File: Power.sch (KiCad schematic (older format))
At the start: 21 parts, among them Q1 DMG3405, U6 MCP73831-2-OT, U7 TPS737xx

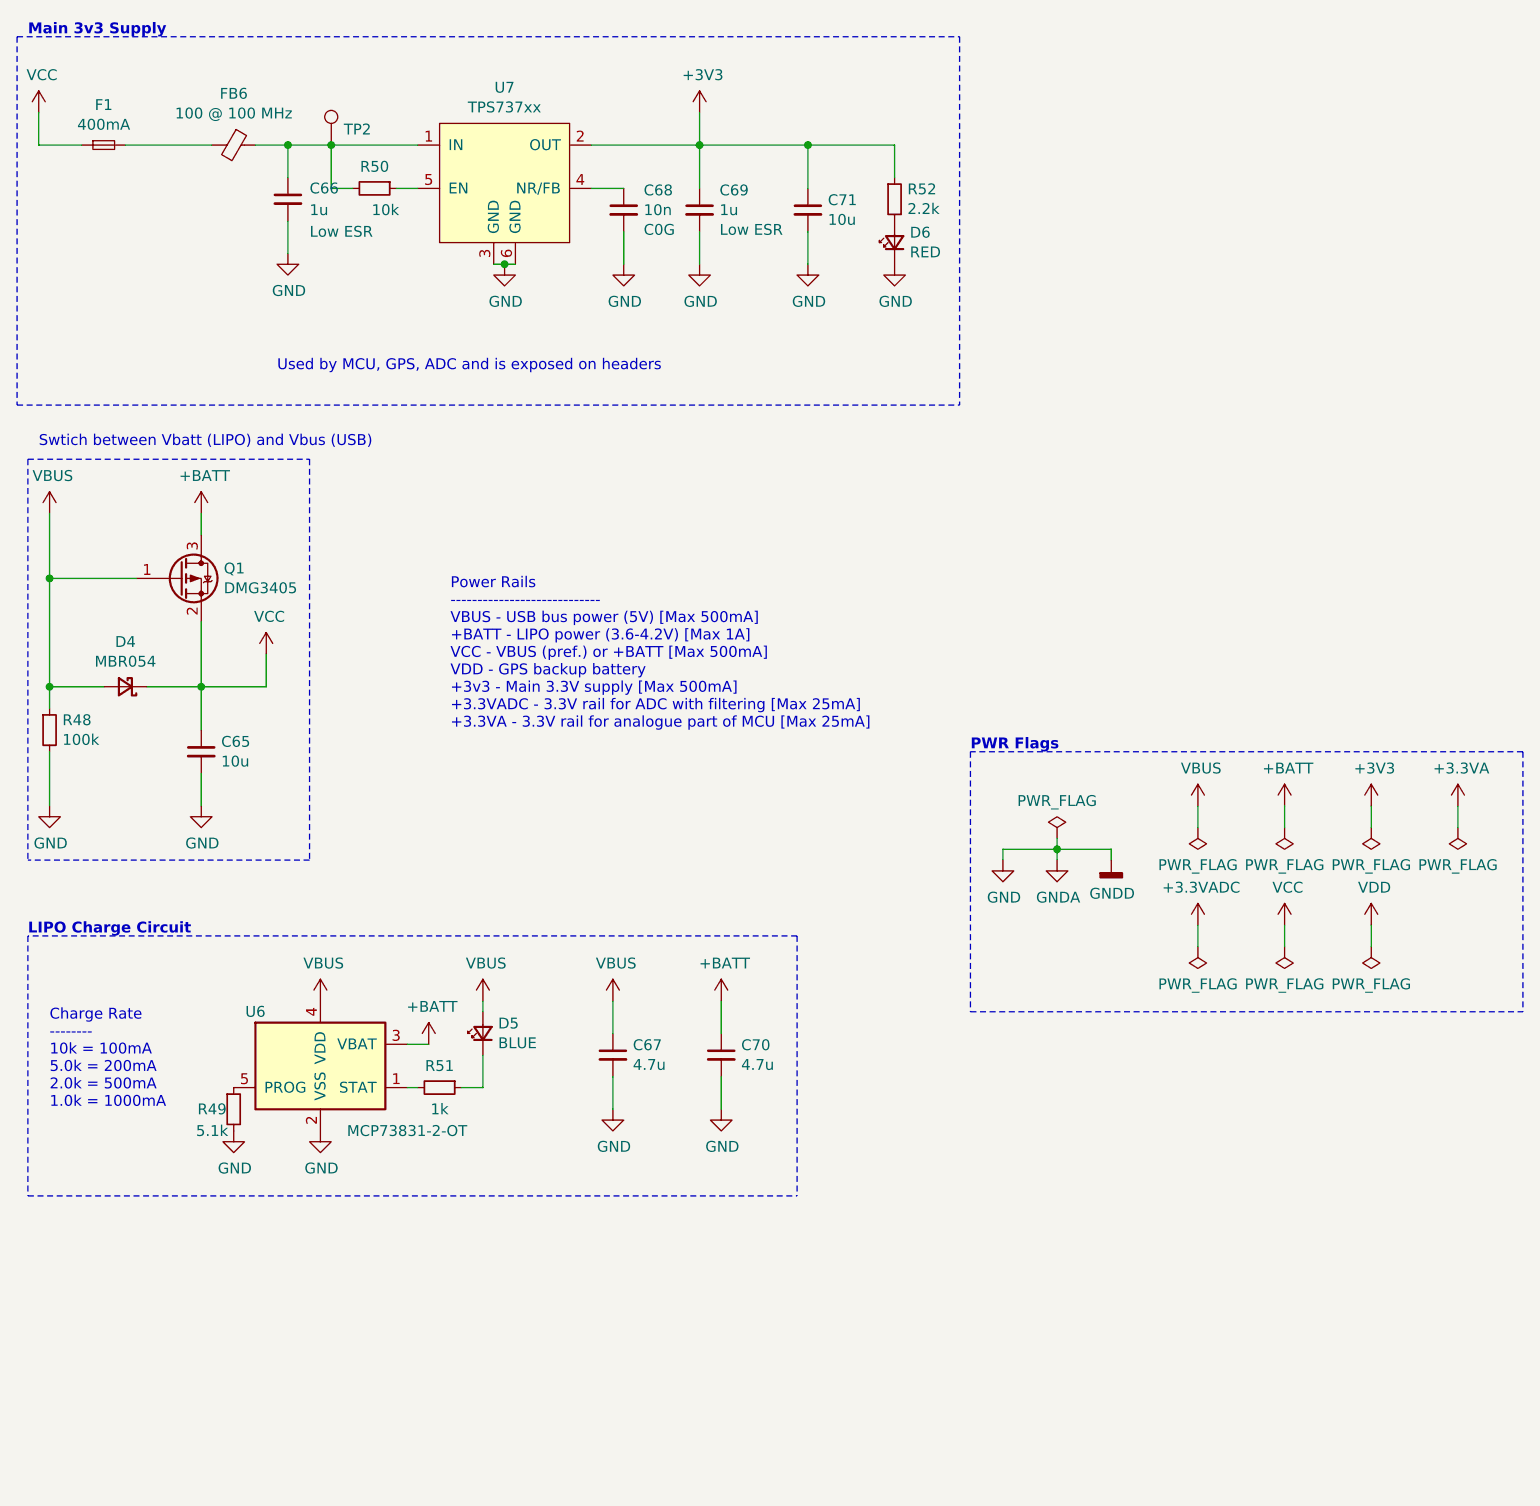
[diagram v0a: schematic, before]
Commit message: Assign footprints for all components
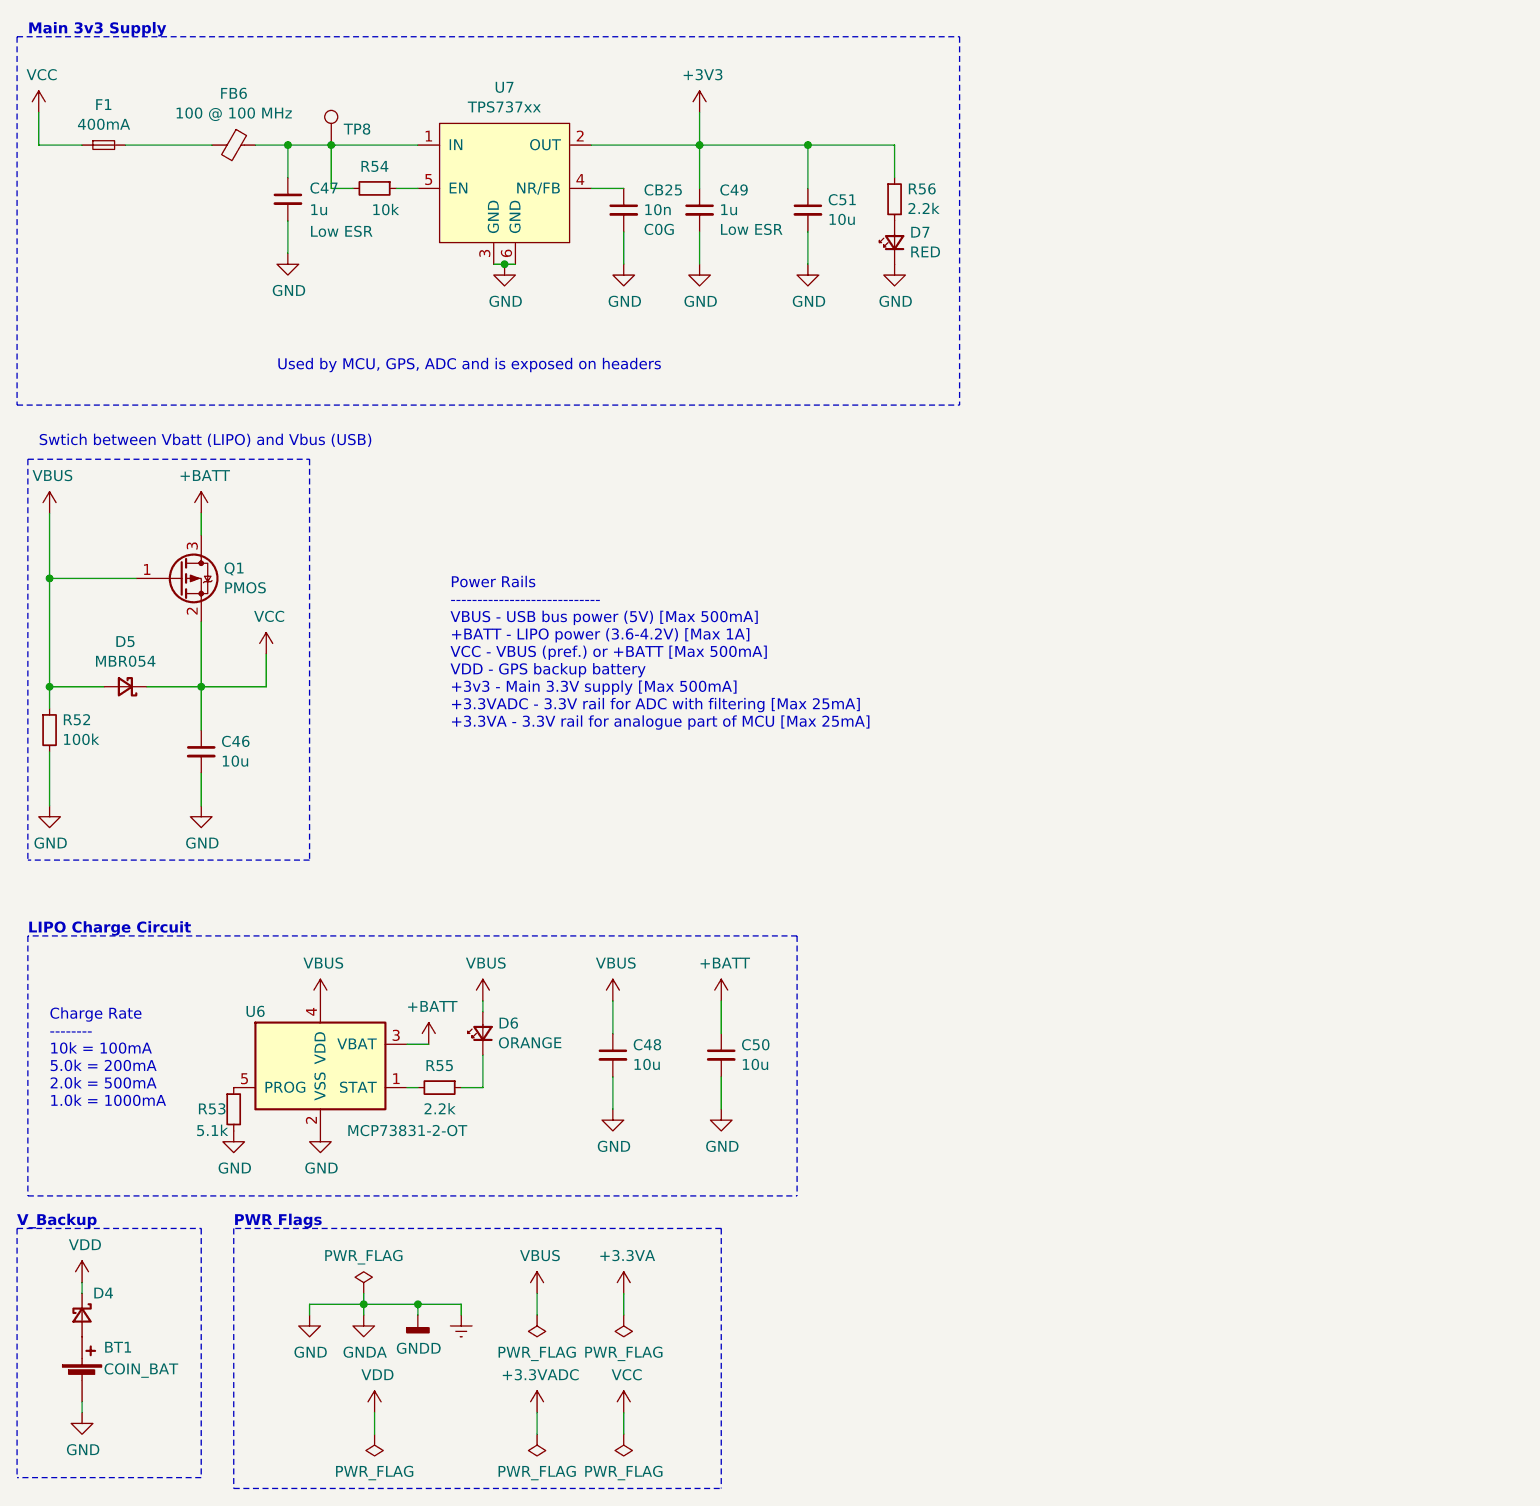
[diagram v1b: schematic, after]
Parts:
- removed C67, C70: 4.7u, symbol Device:C_Small
- added BT1: COIN_BAT, Battery:BatteryHolder_Keystone_3002_1x2032, symbol Device:Battery_Cell
- added C48, C50: 10u, Capacitor_SMD:C_0805_2012Metric_Pad1.15x1.40mm_HandSolder, symbol Device:C_Small
- added D4: ~, Diode_SMD:D_SOD-123, symbol Device:D_Schottky_Small
- C46: renamed from C65; footprint (none) -> Capacitor_SMD:C_0805_2012Metric_Pad1.15x1.40mm_HandSolder
- C47: renamed from C66; footprint (none) -> Capacitor_SMD:C_0603_1608Metric_Pad1.05x0.95mm_HandSolder; MPN (none) -> C0603C105K8RACTU; Mfr. (none) -> KEMET
- C49: renamed from C69; footprint (none) -> Capacitor_SMD:C_0603_1608Metric_Pad1.05x0.95mm_HandSolder; MPN (none) -> C0603C105K8RACTU; Mfr. (none) -> KEMET
- C51: renamed from C71; footprint (none) -> Capacitor_SMD:C_0805_2012Metric_Pad1.15x1.40mm_HandSolder
- CB25: renamed from C68; footprint (none) -> Capacitor_SMD:C_0603_1608Metric_Pad1.05x0.95mm_HandSolder
- D5: renamed from D4; footprint (none) -> Diode_SMD:D_SOD-123; MPN MBR054 -> MBR0540T3G; Mfr. (none) -> ON Semiconductor
- D6: renamed from D5; value BLUE -> ORANGE; footprint (none) -> LED_SMD:LED_0603_1608Metric_Pad1.05x0.95mm_HandSolder; MPN (none) -> SML-D12D8WT86C; Mfr. (none) -> ROHM Semiconductor
- D7: renamed from D6; footprint (none) -> LED_SMD:LED_0603_1608Metric_Pad1.05x0.95mm_HandSolder; MPN (none) -> SML-D12U8WT86C; Mfr. (none) -> ROHM Semiconductor
- F1: footprint (none) -> Fuse:Fuse_0603_1608Metric_Pad1.05x0.95mm_HandSolder; MPN (none) -> 0686F0500-01; Mfr. (none) -> Bel Fuse
- FB6: footprint (none) -> Inductor_SMD:L_0603_1608Metric_Pad1.05x0.95mm_HandSolder; MPN (none) -> BLM18EG101TZ1D; Mfr. (none) -> Murata Electronics
- Q1: value DMG3405 -> PMOS; footprint (none) -> Package_TO_SOT_SMD:SOT-23_Handsoldering; MPN DMG3405 -> NTR3A30PZT1G; Mfr. (none) -> ON Semiconductor; Notes (none) -> Low Rds_on; Low Gate Voltage
- R52: renamed from R48; footprint (none) -> Resistor_SMD:R_0603_1608Metric_Pad1.05x0.95mm_HandSolder; MPN (none) -> RC0603FR-07100KL; Mfr. (none) -> Yageo
- R53: renamed from R49; footprint (none) -> Resistor_SMD:R_0603_1608Metric_Pad1.05x0.95mm_HandSolder; MPN (none) -> AC0603FR-135K1L; Mfr. (none) -> Yageo
- R54: renamed from R50; footprint (none) -> Resistor_SMD:R_0603_1608Metric_Pad1.05x0.95mm_HandSolder
- R55: renamed from R51; value 1k -> 2.2k; footprint (none) -> Resistor_SMD:R_0603_1608Metric_Pad1.05x0.95mm_HandSolder
- R56: renamed from R52; footprint (none) -> Resistor_SMD:R_0603_1608Metric_Pad1.05x0.95mm_HandSolder
- TP8: renamed from TP2; footprint (none) -> TestPoint:TestPoint_Pad_D1.0mm
- U7: footprint (none) -> grootvoet:TPS737
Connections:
- net +BATT: now also C50.1
- net VBUS: now also C48.1
- net VDD: now also D4.1 (K)
- net GND renamed Earth
- net Earth: now also BT1.2 (-), C48.2, C50.2
- new net: BT1.1 (+), D4.2 (A)
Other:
- note added: "V_Backup"

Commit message: Change voltage polarity diode
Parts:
- removed D4: ~, Diode_SMD:D_SOD-123, symbol Device:D_Schottky_Small
- added D?: Vf low, Diode_SMD:D_SOD-123, symbol Device:D_Schottky_Small
- D5: value MBR054 -> Vf low; MPN MBR0540T3G -> RSX101MM-30TR; Mfr. ON Semiconductor -> ROHM Semiconductor
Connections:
- net VDD: now also D?.1 (K)
- net at BT1.1 (+): now also D?.2 (A)
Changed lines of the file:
@@
-$EndComp
-$Comp
-L Device:D_Schottky_Small D5
-U 1 1 5EEDF9F3
-P 4050 3950
-F 0 "D5" H 4050 3743 50  0000 C CNN
-F 1 "MBR054" H 4050 3834 50  0000 C CNN
-F 2 "Diode_SMD:D_SOD-123" V 4050 3950 50  0001 C CNN
-F 3 "~" V 4050 3950 50  0001 C CNN
-F 4 "MBR0540T3G" H 4050 3950 50  0001 C CNN "MPN"
-F 5 "ON Semiconductor" H 4050 3950 50  0001 C CNN "Mfr."
-	1    4050 3950
-	-1   0    0    1
 $EndComp
 $Comp
@@
 	1    0    0    -1
 $EndComp
-$Comp
-L Device:D_Schottky_Small D?
-U 1 1 5EEC591B
-P 3850 6850
-AR Path="/5EEC591B" Ref="D?"  Part="1"
-AR Path="/5EDF3693/5EEC591B" Ref="D?"  Part="1"
-AR Path="/5EEDE770/5EEC591B" Ref="D4"  Part="1"
-F 0 "D4" V 3750 6900 50  0000 L CNN
-F 1 "~" V 3850 6150 50  0000 L CNN
-F 2 "Diode_SMD:D_SOD-123" V 3850 6850 50  0001 C CNN
-F 3 "~" V 3850 6850 50  0001 C CNN
-F 4 "MBR0540T3G" V 3850 6850 50  0001 C CNN "MPN"
-F 5 "ON Semiconductor" V 3850 6850 50  0001 C CNN "Mfr."
-	1    3850 6850
-	0    1    1    0
-$EndComp
 Wire Wire Line
 	3850 7300 3850 7250
@@
 	1    0    0    -1
 $EndComp
+$Comp
+L Device:D_Schottky_Small D5
+U 1 1 5EF173D0
+P 4050 3950
+AR Path="/5EEDE770/5EF173D0" Ref="D5"  Part="1"
+AR Path="/5EDF3693/5EF173D0" Ref="D?"  Part="1"
+F 0 "D5" H 4050 3743 50  0000 C CNN
+F 1 "Vf low" H 4050 3834 50  0000 C CNN
+F 2 "Diode_SMD:D_SOD-123" V 4050 3950 50  0001 C CNN
+F 3 "~" V 4050 3950 50  0001 C CNN
+F 4 "RSX101MM-30TR" H 4050 3950 50  0001 C CNN "MPN"
+F 5 "ROHM Semiconductor" H 4050 3950 50  0001 C CNN "Mfr."
+	1    4050 3950
+	-1   0    0    1
+$EndComp
+$Comp
+L Device:D_Schottky_Small D?
+U 1 1 5EF1F889
+P 3850 6850
+AR Path="/5EEDE770/5EF1F889" Ref="D?"  Part="1"
+AR Path="/5EDF3693/5EF1F889" Ref="D?"  Part="1"
+F 0 "D?" H 3850 6643 50  0000 C CNN
+F 1 "Vf low" H 3850 6734 50  0000 C CNN
+F 2 "Diode_SMD:D_SOD-123" V 3850 6850 50  0001 C CNN
+F 3 "~" V 3850 6850 50  0001 C CNN
+F 4 "RSX101MM-30TR" H 3850 6850 50  0001 C CNN "MPN"
+F 5 "ROHM Semiconductor" H 3850 6850 50  0001 C CNN "Mfr."
+	1    3850 6850
+	0    1    1    0
+$EndComp
 $EndSCHEMATC
